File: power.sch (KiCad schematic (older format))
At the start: 41 parts, among them Q2 AO3401, SW9 SW_SPDT_shielded, U5 M3406, U6 XC6206P25, U7 XR1151, U9 XR1151

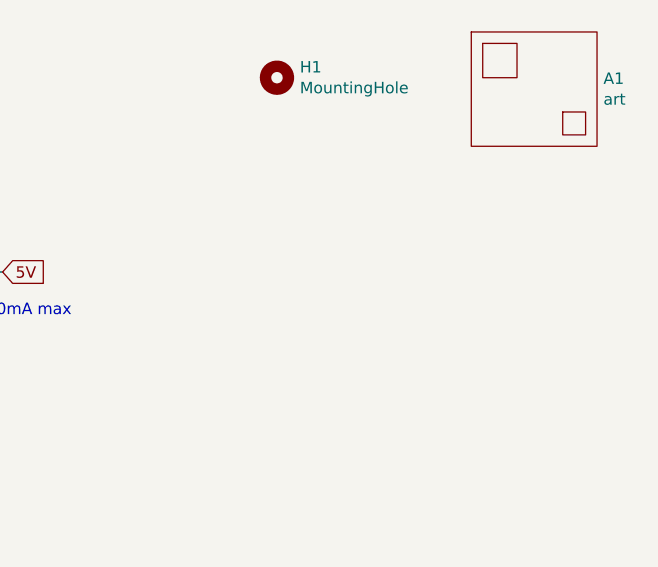
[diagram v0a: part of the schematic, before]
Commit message: Final changes: add some fiducials, clean up vias. Ready for prod, I hope.
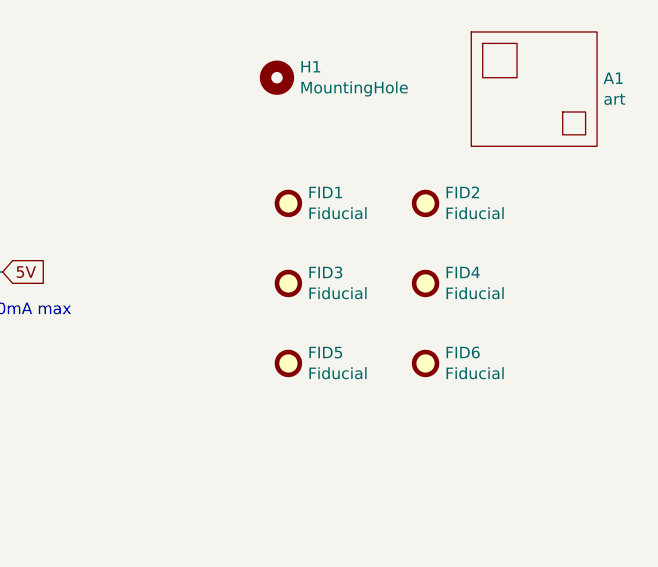
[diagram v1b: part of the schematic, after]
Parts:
- added FID1, FID2, FID3, FID4, FID5, FID6: Fiducial, Fiducial:Fiducial_0.75mm_Mask1.5mm, symbol Mechanical:Fiducial
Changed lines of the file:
@@
+	1    0    0    -1
+$EndComp
+$Comp
+L Mechanical:Fiducial FID1
+U 1 1 5D8D7810
+P 6400 5650
+F 0 "FID1" H 6485 5696 50  0000 L CNN
+F 1 "Fiducial" H 6485 5605 50  0000 L CNN
+F 2 "Fiducial:Fiducial_0.75mm_Mask1.5mm" H 6400 5650 50  0001 C CNN
+F 3 "~" H 6400 5650 50  0001 C CNN
+	1    6400 5650
+	1    0    0    -1
+$EndComp
+$Comp
+L Mechanical:Fiducial FID2
+U 1 1 5D8D81BD
+P 7000 5650
+F 0 "FID2" H 7085 5696 50  0000 L CNN
+F 1 "Fiducial" H 7085 5605 50  0000 L CNN
+F 2 "Fiducial:Fiducial_0.75mm_Mask1.5mm" H 7000 5650 50  0001 C CNN
+F 3 "~" H 7000 5650 50  0001 C CNN
+	1    7000 5650
+	1    0    0    -1
+$EndComp
+$Comp
+L Mechanical:Fiducial FID3
+U 1 1 5D8E19E9
+P 6400 6000
+F 0 "FID3" H 6485 6046 50  0000 L CNN
+F 1 "Fiducial" H 6485 5955 50  0000 L CNN
+F 2 "Fiducial:Fiducial_0.75mm_Mask1.5mm" H 6400 6000 50  0001 C CNN
+F 3 "~" H 6400 6000 50  0001 C CNN
+	1    6400 6000
+	1    0    0    -1
+$EndComp
+$Comp
+L Mechanical:Fiducial FID4
+U 1 1 5D8E19EF
+P 7000 6000
+F 0 "FID4" H 7085 6046 50  0000 L CNN
+F 1 "Fiducial" H 7085 5955 50  0000 L CNN
+F 2 "Fiducial:Fiducial_0.75mm_Mask1.5mm" H 7000 6000 50  0001 C CNN
+F 3 "~" H 7000 6000 50  0001 C CNN
+	1    7000 6000
+	1    0    0    -1
+$EndComp
+$Comp
+L Mechanical:Fiducial FID5
+U 1 1 5D8E7160
+P 6400 6350
+F 0 "FID5" H 6485 6396 50  0000 L CNN
+F 1 "Fiducial" H 6485 6305 50  0000 L CNN
+F 2 "Fiducial:Fiducial_0.75mm_Mask1.5mm" H 6400 6350 50  0001 C CNN
+F 3 "~" H 6400 6350 50  0001 C CNN
+	1    6400 6350
+	1    0    0    -1
+$EndComp
+$Comp
+L Mechanical:Fiducial FID6
+U 1 1 5D8E7166
+P 7000 6350
+F 0 "FID6" H 7085 6396 50  0000 L CNN
+F 1 "Fiducial" H 7085 6305 50  0000 L CNN
+F 2 "Fiducial:Fiducial_0.75mm_Mask1.5mm" H 7000 6350 50  0001 C CNN
+F 3 "~" H 7000 6350 50  0001 C CNN
+	1    7000 6350
 	1    0    0    -1
 $EndComp
